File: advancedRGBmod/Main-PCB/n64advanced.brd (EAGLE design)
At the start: 64.5 x 37.7 mm, 112 parts, among them J6 UPS, U1 10CL010YE144, U2 ADV7125/ADV7123, U4 74LVC3G17, U5 S25FLXXXSO8-DUAL, U6 TLV70012DDC, U7 TLV70025DDC

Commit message: Add filter bypass option for FilterAddOn; e.g. for simple signal conversion for PAL SNES RGB cables
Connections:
- net NC renamed FIL_BYPASS
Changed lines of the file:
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@@
 <?xml version="1.0" encoding="utf-8"?>
 <!DOCTYPE eagle SYSTEM "eagle.dtd">
-<eagle version="8.4.2">
+<eagle version="8.4.3">
 <drawing>
 <settings>
@@
 <wire x1="30.226" y1="30.988" x2="29.502153125" y2="30.988" width="0.2032" layer="1"/>
 </signal>
-<signal name="NC">
+<signal name="FIL_BYPASS">
 <contactref element="J1" pad="1"/>
 <contactref element="U1" pad="112"/>

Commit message: update resistor value
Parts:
- R21: value 530/560 -> 518/515
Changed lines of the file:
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@@
 <element name="R16" library="rcl" package="R0603" value="10k" x="39.497" y="29.21" smashed="yes" rot="R270"/>
 <element name="R51" library="rcl" package="R0603" value="25" x="10.16" y="11.303" smashed="yes" rot="MR180"/>
-<element name="R21" library="rcl" package="R0603" value="530/560" x="53.34" y="19.05" smashed="yes" rot="MR0"/>
+<element name="R21" library="rcl" package="R0603" value="518/515" x="53.34" y="19.05" smashed="yes" rot="MR0"/>
 <element name="R22" library="rcl" package="R0603" value="4k7" x="54.864" y="21.844" smashed="yes" rot="MR90"/>
 <element name="R53" library="rcl" package="R0603" value="4k7" x="10.16" y="15.367" smashed="yes" rot="MR180"/>

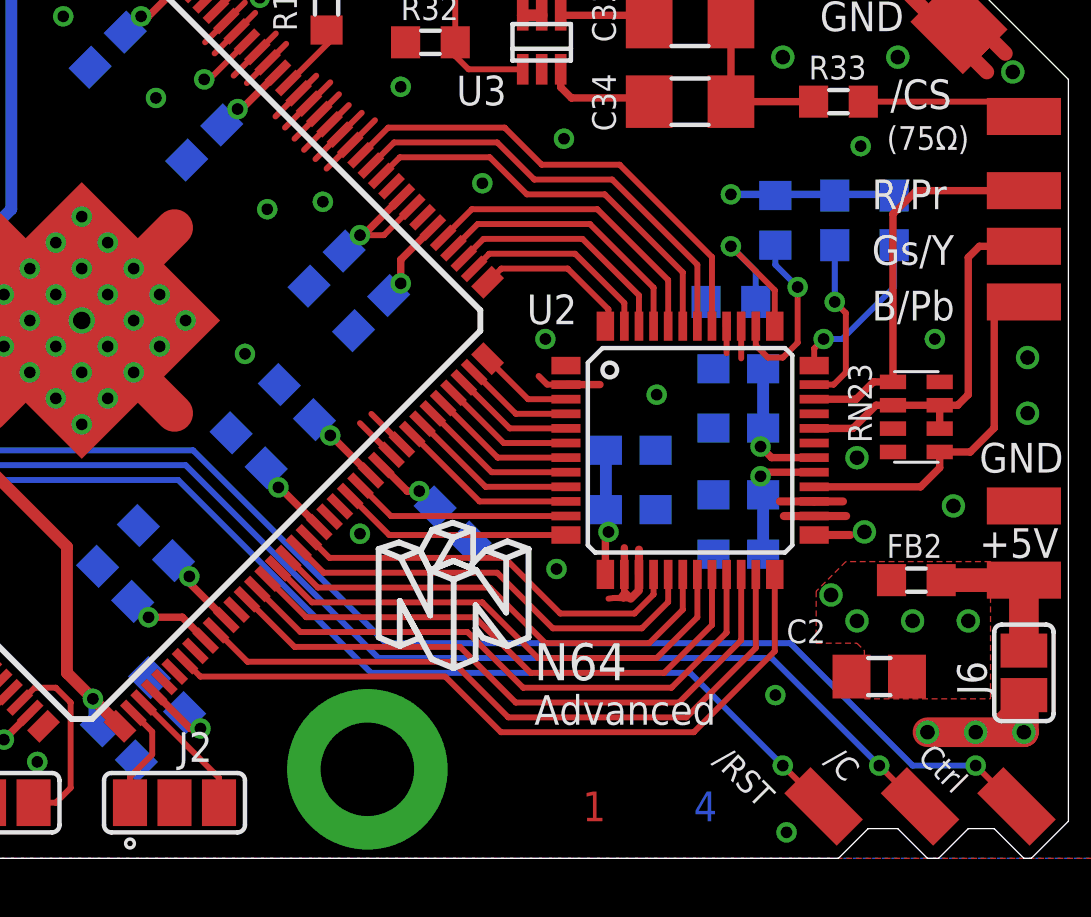
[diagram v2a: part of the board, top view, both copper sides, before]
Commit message: Place R21 (R_set of the DAC) on TOP layer making it easy to replace if board is installed
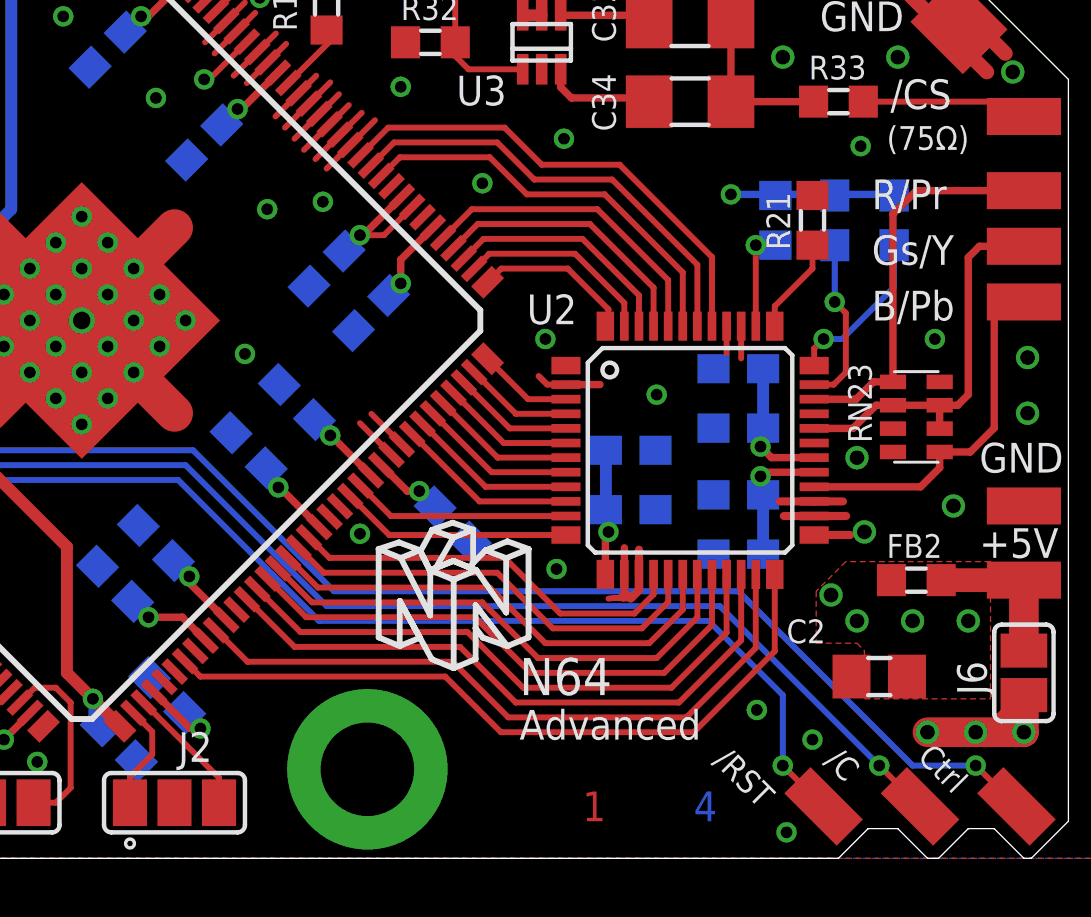
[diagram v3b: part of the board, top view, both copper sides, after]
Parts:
- moved R21 3.95 mm to (56.1, 21.8), flipped to the top, turned to 90 degrees
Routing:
- net N$22: track 6.13 -> 3.45 mm
- net N$2: track 5.61 -> 3.31 mm, vias 1 -> 0
- net N$70: track 61.7 -> 63.1 mm
- net GND: vias 85 -> 86
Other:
- board text added: "N64A_20171204"
- board text removed: "N64A_20171019"
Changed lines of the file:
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@@
 <layers>
 <layer number="1" name="Top" color="4" fill="1" visible="yes" active="yes"/>
-<layer number="2" name="Route2" color="1" fill="3" visible="no" active="yes"/>
+<layer number="2" name="Route2" color="1" fill="3" visible="yes" active="yes"/>
 <layer number="3" name="Route3" color="4" fill="3" visible="no" active="no"/>
 <layer number="4" name="Route4" color="1" fill="4" visible="no" active="no"/>
@@
 <text x="56.515" y="23.495" size="0.8128" layer="26" font="vector" ratio="15" rot="MR90">C22</text>
 <text x="54.356" y="23.495" size="0.8128" layer="26" font="vector" ratio="15" rot="MR90">R22</text>
-<text x="51.689" y="18.669" size="0.8128" layer="26" font="vector" ratio="15" rot="MR0">R21</text>
+<text x="55.372" y="20.828" size="0.8128" layer="25" font="vector" ratio="15" rot="R90">R21</text>
 <text x="48.26" y="12.573" size="0.8128" layer="26" font="vector" ratio="15" rot="MR0">C201</text>
 <text x="48.387" y="14.605" size="0.8128" layer="26" font="vector" ratio="15" rot="MR0">C202</text>
@@
 <vertex x="47.8282" y="0.8382"/>
 </polygon>
-<text x="46.609" y="4.572" size="1.016" layer="21" font="vector" ratio="15">Advanced</text>
-<text x="46.609" y="6.096" size="1.27" layer="21" font="vector" ratio="15">N64</text>
+<text x="46.101" y="4.064" size="1.016" layer="21" font="vector" ratio="15">Advanced</text>
+<text x="46.101" y="5.588" size="1.27" layer="21" font="vector" ratio="15">N64</text>
 <text x="16.129" y="24.892" size="1.016" layer="21" font="vector" ratio="15" align="center">__/)__/)_</text>
 <wire x1="51.308" y1="30.353" x2="52.578" y2="30.353" width="0.1524" layer="21"/>
@@
 <circle x="32.766" y="0.508" radius="0.05679375" width="0.3048" layer="25"/>
 <circle x="29.464" y="37.211" radius="0.05679375" width="0.3048" layer="25"/>
-<text x="10.668" y="1.27" size="1.016" layer="26" font="vector" ratio="12" rot="MR0" align="center">N64A_20171019</text>
+<text x="10.668" y="1.27" size="1.016" layer="26" font="vector" ratio="12" rot="MR0" align="center">N64A_20171204</text>
 <wire x1="11.303" y1="30.861" x2="11.303" y2="33.909" width="0.1524" layer="25"/>
 <wire x1="11.303" y1="33.909" x2="12.573" y2="35.179" width="0.1524" layer="25"/>
@@
 <element name="R16" library="rcl" package="R0603" value="10k" x="39.497" y="29.21" smashed="yes" rot="R270"/>
 <element name="R51" library="rcl" package="R0603" value="25" x="10.16" y="11.303" smashed="yes" rot="MR180"/>
-<element name="R21" library="rcl" package="R0603" value="518/515" x="53.34" y="19.05" smashed="yes" rot="MR0"/>
+<element name="R21" library="rcl" package="R0603" value="518/515" x="56.134" y="21.844" smashed="yes" rot="R90"/>
 <element name="R22" library="rcl" package="R0603" value="4k7" x="54.864" y="21.844" smashed="yes" rot="MR90"/>
 <element name="R53" library="rcl" package="R0603" value="4k7" x="10.16" y="15.367" smashed="yes" rot="MR180"/>
@@
 <wire x1="37.76040625" y1="28.2423875" x2="37.12540625" y2="27.6073875" width="0.2032" layer="1"/>
 <wire x1="38.113959375" y1="27.888834375" x2="37.478959375" y2="27.253834375" width="0.2032" layer="1"/>
-<via x="54.864" y="5.588" extent="1-16" drill="0.4"/>
+<via x="56.134" y="4.064" extent="1-16" drill="0.4"/>
 <wire x1="53.193" y1="17.292" x2="53.193" y2="18.22" width="0.2032" layer="1"/>
 <wire x1="53.693" y1="17.117" x2="53.693" y2="18.22" width="0.2032" layer="1"/>
@@
 <wire x1="60.833" y1="28.194" x2="62.103" y2="26.924" width="0.508" layer="1"/>
 <via x="37.211" y="29.464" extent="1-16" drill="0.4"/>
+<via x="54.229" y="5.08" extent="1-16" drill="0.4"/>
 </signal>
 <signal name="N$54">
@@
 <contactref element="U2" pad="37"/>
 <contactref element="R21" pad="1"/>
-<wire x1="54.843" y1="18.22" x2="54.843" y2="19.452" width="0.2032" layer="1"/>
-<via x="53.34" y="20.955" extent="1-16" drill="0.4"/>
-<wire x1="53.34" y1="20.955" x2="54.19" y2="20.105" width="0.2032" layer="16"/>
-<wire x1="54.19" y1="20.105" x2="54.19" y2="19.05" width="0.2032" layer="16"/>
-<wire x1="54.843" y1="19.452" x2="53.34" y2="20.955" width="0.2032" layer="1"/>
+<wire x1="54.843" y1="18.22" x2="54.843" y2="18.902" width="0.2032" layer="1"/>
+<wire x1="54.843" y1="18.902" x2="56.134" y2="20.193" width="0.2032" layer="1"/>
+<wire x1="56.134" y1="20.193" x2="56.134" y2="20.994" width="0.2032" layer="1"/>
 </signal>
 <signal name="N$22">
 <contactref element="U2" pad="38"/>
 <contactref element="R22" pad="1"/>
-<wire x1="54.193" y1="18.22" x2="54.193" y2="17.562" width="0.2032" layer="1"/>
-<wire x1="54.193" y1="17.562" x2="54.61" y2="17.145" width="0.2032" layer="1"/>
-<wire x1="54.61" y1="17.145" x2="55.118" y2="17.145" width="0.2032" layer="1"/>
-<wire x1="55.118" y1="17.145" x2="55.626" y2="17.653" width="0.2032" layer="1"/>
-<wire x1="55.626" y1="17.653" x2="55.626" y2="19.558" width="0.2032" layer="1"/>
-<via x="55.626" y="19.558" extent="1-16" drill="0.4"/>
-<wire x1="55.626" y1="19.558" x2="54.864" y2="20.32" width="0.2032" layer="16"/>
-<wire x1="54.864" y1="20.32" x2="54.864" y2="20.994" width="0.2032" layer="16"/>
+<wire x1="54.193" y1="18.22" x2="54.193" y2="20.994" width="0.2032" layer="1"/>
+<via x="54.193" y="20.994" extent="1-16" drill="0.4"/>
+<wire x1="54.193" y1="20.994" x2="54.268" y2="20.994" width="0.2032" layer="16"/>
+<wire x1="54.268" y1="20.994" x2="54.864" y2="20.994" width="0.2032" layer="16"/>
 </signal>
 <signal name="N$23">
@@
 <wire x1="63.119" y1="1.778" x2="61.722" y2="3.175" width="0.2032" layer="1"/>
 <via x="61.722" y="3.175" extent="1-16" drill="0.4"/>
-<wire x1="55.372" y1="7.366" x2="41.529" y2="7.366" width="0.2032" layer="16"/>
+<wire x1="53.594" y1="9.144" x2="39.751" y2="9.144" width="0.2032" layer="16"/>
 <via x="5.969" y="26.67" extent="1-16" drill="0.4"/>
 <wire x1="5.969" y1="26.67" x2="6.039" y2="26.6" width="0.2032" layer="1"/>
 <wire x1="6.039" y1="26.6" x2="7.455" y2="26.6" width="0.2032" layer="1"/>
-<wire x1="34.925" y1="13.97" x2="41.529" y2="7.366" width="0.2032" layer="16"/>
+<wire x1="34.925" y1="13.97" x2="39.751" y2="9.144" width="0.2032" layer="16"/>
 <wire x1="8.636" y1="24.638" x2="13.081" y2="24.638" width="0.2032" layer="16"/>
 <wire x1="8.636" y1="24.638" x2="6.604" y2="26.67" width="0.2032" layer="16"/>
 <wire x1="6.604" y1="26.67" x2="5.969" y2="26.67" width="0.2032" layer="16"/>
 <wire x1="61.722" y1="3.175" x2="59.563" y2="3.175" width="0.2032" layer="16"/>
-<wire x1="59.563" y1="3.175" x2="55.372" y2="7.366" width="0.2032" layer="16"/>
+<wire x1="59.563" y1="3.175" x2="53.594" y2="9.144" width="0.2032" layer="16"/>
 <wire x1="13.081" y1="24.638" x2="20.955" y2="16.764" width="0.2032" layer="16"/>
 <wire x1="24.384" y1="16.764" x2="27.178" y2="13.97" width="0.2032" layer="16"/>
@@
 <via x="58.42" y="3.175" extent="1-16" drill="0.4"/>
 <via x="4.445" y="26.67" extent="1-16" drill="0.4"/>
-<wire x1="34.671" y1="13.462" x2="41.275" y2="6.858" width="0.2032" layer="16"/>
-<wire x1="58.42" y1="3.175" x2="54.737" y2="6.858" width="0.2032" layer="16"/>
-<wire x1="54.737" y1="6.858" x2="41.275" y2="6.858" width="0.2032" layer="16"/>
+<wire x1="34.671" y1="13.462" x2="39.497" y2="8.636" width="0.2032" layer="16"/>
+<wire x1="58.42" y1="3.175" x2="52.959" y2="8.636" width="0.2032" layer="16"/>
+<wire x1="52.959" y1="8.636" x2="39.497" y2="8.636" width="0.2032" layer="16"/>
 <wire x1="5.334" y1="25.781" x2="4.445" y2="26.67" width="0.2032" layer="16"/>
 <wire x1="4.445" y1="26.67" x2="5.315" y2="25.8" width="0.2032" layer="1"/>
@@
 <wire x1="56.515" y1="1.778" x2="55.118" y2="3.175" width="0.2032" layer="1"/>
 <via x="55.118" y="3.175" extent="1-16" drill="0.4"/>
-<wire x1="55.118" y1="3.175" x2="51.943" y2="6.35" width="0.2032" layer="16"/>
 <via x="5.969" y="25.019" extent="1-16" drill="0.4"/>
 <wire x1="5.969" y1="25.019" x2="5.988" y2="25" width="0.2032" layer="1"/>
 <wire x1="5.988" y1="25" x2="7.455" y2="25" width="0.2032" layer="1"/>
-<wire x1="51.943" y1="6.35" x2="41.021" y2="6.35" width="0.2032" layer="16"/>
-<wire x1="34.417" y1="12.954" x2="41.021" y2="6.35" width="0.2032" layer="16"/>
+<wire x1="39.243" y1="8.128" x2="34.417" y2="12.954" width="0.2032" layer="16"/>
 <wire x1="7.366" y1="23.622" x2="12.573" y2="23.622" width="0.2032" layer="16"/>
 <wire x1="7.366" y1="23.622" x2="5.969" y2="25.019" width="0.2032" layer="16"/>
@@
 <wire x1="26.67" y1="12.954" x2="34.417" y2="12.954" width="0.2032" layer="16"/>
 <wire x1="20.447" y1="15.748" x2="23.876" y2="15.748" width="0.2032" layer="16"/>
+<wire x1="55.118" y1="3.175" x2="55.118" y2="5.588" width="0.2032" layer="16"/>
+<wire x1="55.118" y1="5.588" x2="52.578" y2="8.128" width="0.2032" layer="16"/>
+<wire x1="52.578" y1="8.128" x2="39.243" y2="8.128" width="0.2032" layer="16"/>
 </signal>
 <signal name="N$77">
